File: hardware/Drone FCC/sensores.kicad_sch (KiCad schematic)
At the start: 12 parts, among them J1 Mag Dupont, J19 GPS M8N - DF13, J2 GPS Dupont, J20 Mag DF13, U1 ICM-42688-V, U2 ILPS22QSTR

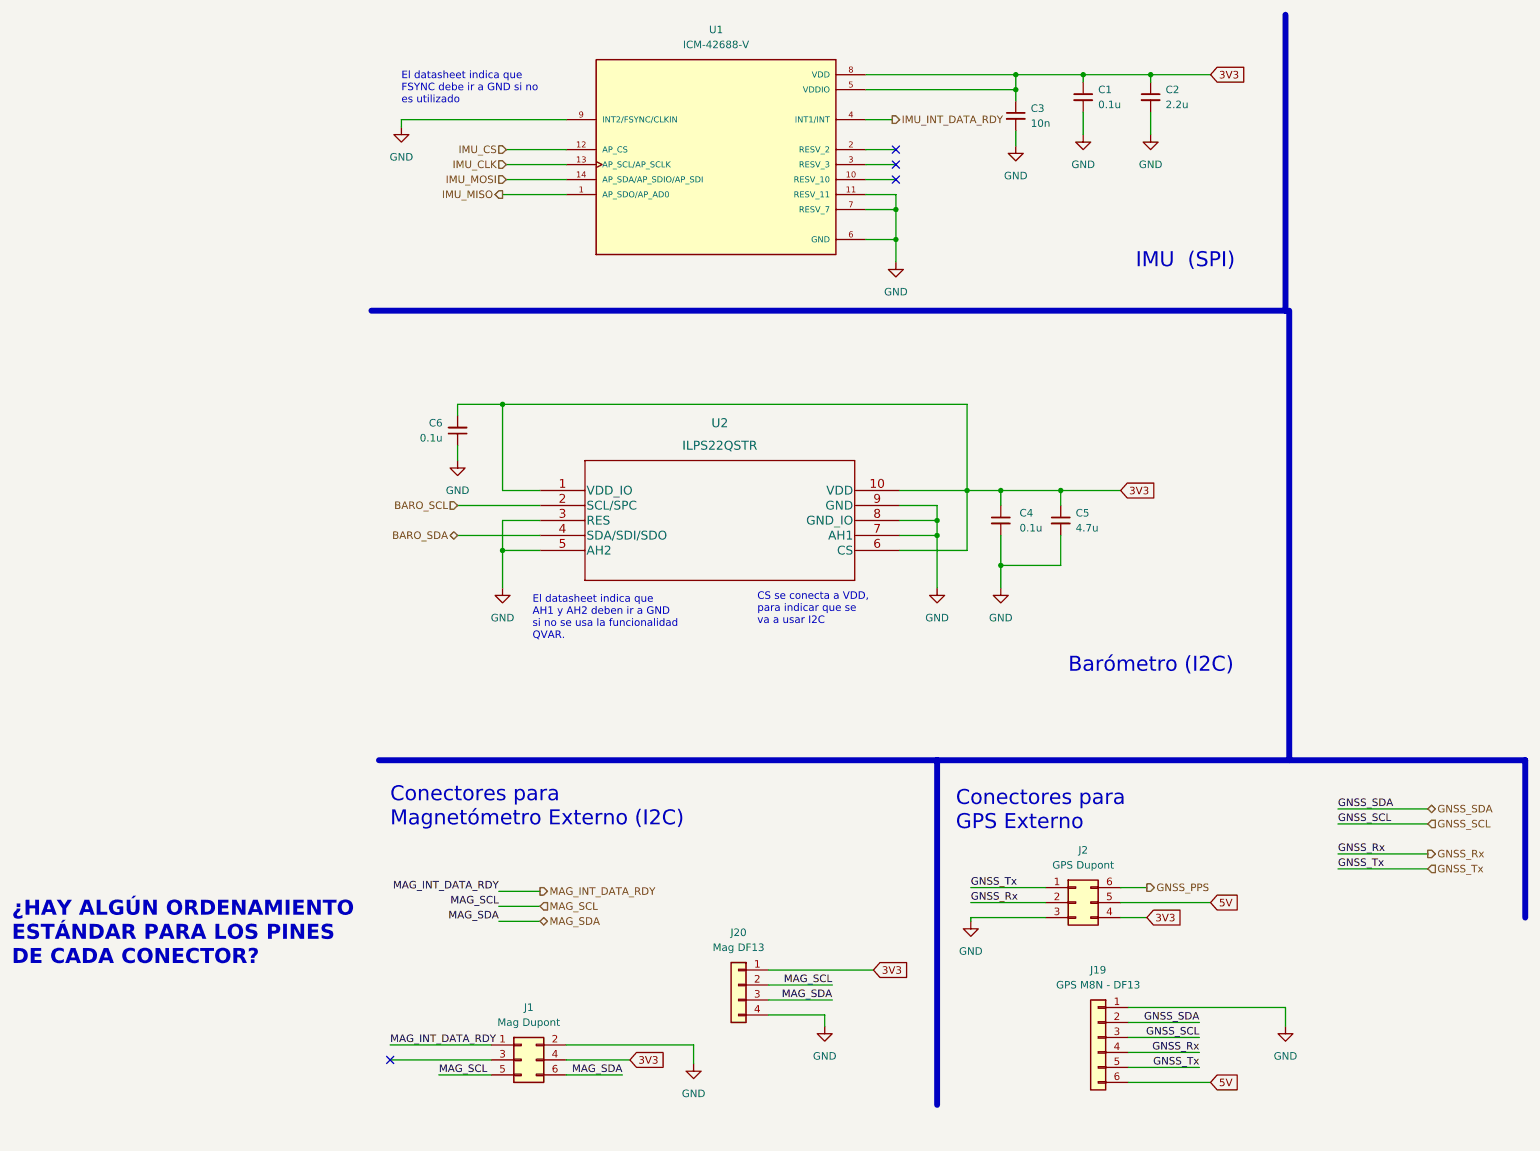
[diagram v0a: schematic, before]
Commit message: re enumeration of components
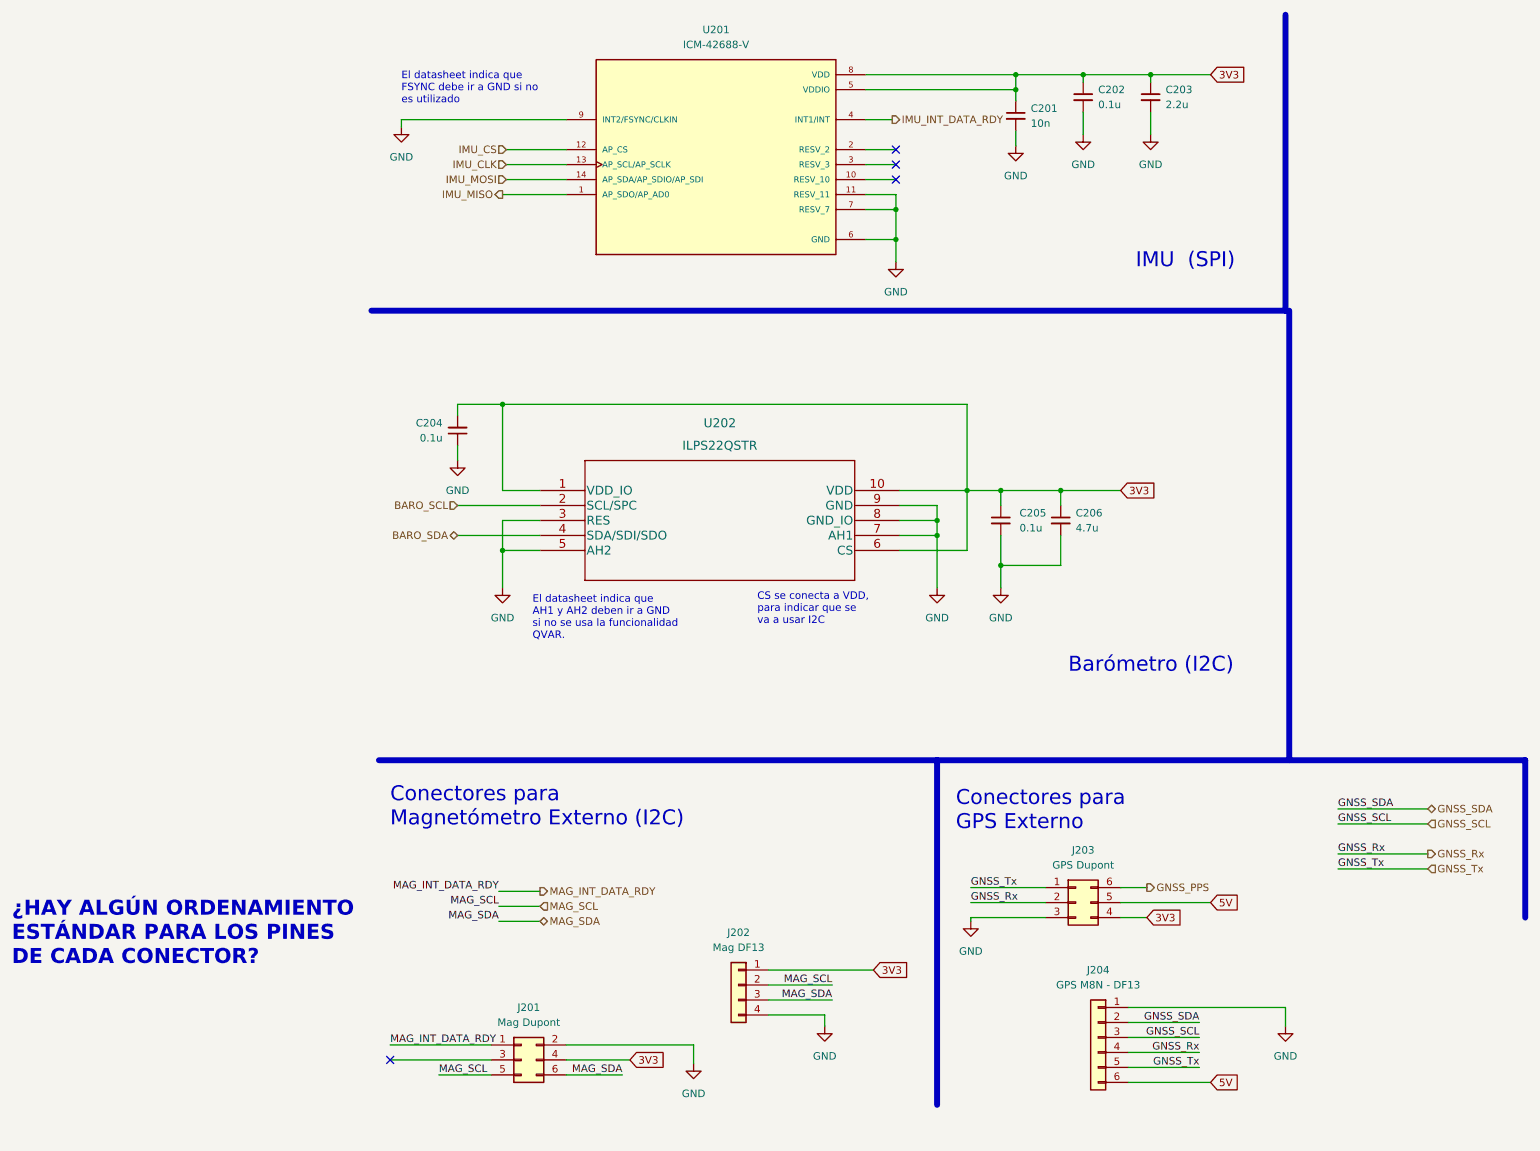
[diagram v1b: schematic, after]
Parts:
- C201: renamed from C3; footprint (none) -> Capacitor_SMD:C_0603_1608Metric_Pad1.08x0.95mm_HandSolder
- C202: renamed from C1; footprint (none) -> Capacitor_SMD:C_0603_1608Metric_Pad1.08x0.95mm_HandSolder
- C203: renamed from C2; footprint (none) -> Capacitor_SMD:C_0603_1608Metric_Pad1.08x0.95mm_HandSolder
- C204: renamed from C6; footprint (none) -> Capacitor_SMD:C_0603_1608Metric_Pad1.08x0.95mm_HandSolder
- C205: renamed from C4; footprint (none) -> Capacitor_SMD:C_0603_1608Metric_Pad1.08x0.95mm_HandSolder
- C206: renamed from C5; footprint (none) -> Capacitor_SMD:C_0805_2012Metric_Pad1.18x1.45mm_HandSolder
- renumbered J1 to J201, J20 to J202, J2 to J203, J19 to J204, U1 to U201, U2 to U202
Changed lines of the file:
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@@
   (symbol (lib_id "Connector_Generic:Conn_02x03_Odd_Even") (at 37.465 189.23 0) (unit 1)
     (in_bom yes) (on_board yes) (fields_autoplaced)
-    (property "Reference" "J1" (id 0) (at 38.735 180.34 0))
+    (property "Reference" "J201" (id 0) (at 38.735 180.34 0))
     (property "Value" "Mag Dupont" (id 1) (at 38.735 182.88 0))
     (property "Footprint" "Connector_PinHeader_2.54mm:PinHeader_2x03_P2.54mm_Horizontal" (id 2) (at 37.465 189.23 0)
@@
   (symbol (lib_id "Device:C_Small") (at 128.905 97.79 0) (unit 1)
     (in_bom yes) (on_board yes) (fields_autoplaced)
-    (property "Reference" "C5" (id 0) (at 131.445 96.5262 0)
+    (property "Reference" "C206" (id 0) (at 131.445 96.5262 0)
       (effects (font (size 1.27 1.27)) (justify left))
     )
@@
       (effects (font (size 1.27 1.27)) (justify left))
     )
-    (property "Footprint" "" (id 2) (at 128.905 97.79 0)
+    (property "Footprint" "Capacitor_SMD:C_0805_2012Metric_Pad1.18x1.45mm_HandSolder" (id 2) (at 128.905 97.79 0)
       (effects (font (size 1.27 1.27)) hide)
     )
@@
   (symbol (lib_id "Connector_Generic:Conn_01x04") (at 74.295 176.53 0) (mirror y) (unit 1)
     (in_bom yes) (on_board yes) (fields_autoplaced)
-    (property "Reference" "J20" (id 0) (at 74.295 167.64 0))
+    (property "Reference" "J202" (id 0) (at 74.295 167.64 0))
     (property "Value" "Mag DF13" (id 1) (at 74.295 170.18 0))
     (property "Footprint" "Connector_Hirose:Hirose_DF13C_CL535-0404-8-51_1x04-1MP_P1.25mm_Vertical" (id 2) (at 74.295 176.53 0)
@@
   (symbol (lib_id "ICM-42688-V:ICM-42688-V") (at 70.485 34.925 0) (unit 1)
     (in_bom yes) (on_board yes) (fields_autoplaced)
-    (property "Reference" "U1" (id 0) (at 70.485 14.605 0))
+    (property "Reference" "U201" (id 0) (at 70.485 14.605 0))
     (property "Value" "ICM-42688-V" (id 1) (at 70.485 17.145 0))
     (property "Footprint" "ICM-42688-V:PQFN50P300X250X97-14N" (id 2) (at 70.485 34.925 0)
@@
   (symbol (lib_id "ILPS22QSTR:ILPS22QSTR") (at 40.64 92.71 0) (unit 1)
     (in_bom yes) (on_board yes) (fields_autoplaced)
-    (property "Reference" "U2" (id 0) (at 71.12 81.28 0)
+    (property "Reference" "U202" (id 0) (at 71.12 81.28 0)
       (effects (font (size 1.524 1.524)))
     )
@@
   (symbol (lib_id "Device:C_Small") (at 144.145 26.035 0) (unit 1)
     (in_bom yes) (on_board yes) (fields_autoplaced)
-    (property "Reference" "C2" (id 0) (at 146.685 24.7712 0)
+    (property "Reference" "C203" (id 0) (at 146.685 24.7712 0)
       (effects (font (size 1.27 1.27)) (justify left))
     )
@@
       (effects (font (size 1.27 1.27)) (justify left))
     )
-    (property "Footprint" "" (id 2) (at 144.145 26.035 0)
+    (property "Footprint" "Capacitor_SMD:C_0603_1608Metric_Pad1.08x0.95mm_HandSolder" (id 2) (at 144.145 26.035 0)
       (effects (font (size 1.27 1.27)) hide)
     )
@@
   (symbol (lib_id "Device:C_Small") (at 132.715 26.035 0) (unit 1)
     (in_bom yes) (on_board yes) (fields_autoplaced)
-    (property "Reference" "C1" (id 0) (at 135.255 24.7712 0)
+    (property "Reference" "C202" (id 0) (at 135.255 24.7712 0)
       (effects (font (size 1.27 1.27)) (justify left))
     )
@@
       (effects (font (size 1.27 1.27)) (justify left))
     )
-    (property "Footprint" "" (id 2) (at 132.715 26.035 0)
+    (property "Footprint" "Capacitor_SMD:C_0603_1608Metric_Pad1.08x0.95mm_HandSolder" (id 2) (at 132.715 26.035 0)
       (effects (font (size 1.27 1.27)) hide)
     )
@@
   (symbol (lib_id "Device:C_Small") (at 26.67 82.55 0) (mirror x) (unit 1)
     (in_bom yes) (on_board yes) (fields_autoplaced)
-    (property "Reference" "C6" (id 0) (at 24.13 81.2735 0)
+    (property "Reference" "C204" (id 0) (at 24.13 81.2735 0)
       (effects (font (size 1.27 1.27)) (justify right))
     )
@@
       (effects (font (size 1.27 1.27)) (justify right))
     )
-    (property "Footprint" "" (id 2) (at 26.67 82.55 0)
+    (property "Footprint" "Capacitor_SMD:C_0603_1608Metric_Pad1.08x0.95mm_HandSolder" (id 2) (at 26.67 82.55 0)
       (effects (font (size 1.27 1.27)) hide)
     )
@@
   (symbol (lib_id "Device:C_Small") (at 121.285 29.21 0) (unit 1)
     (in_bom yes) (on_board yes) (fields_autoplaced)
-    (property "Reference" "C3" (id 0) (at 123.825 27.9462 0)
+    (property "Reference" "C201" (id 0) (at 123.825 27.9462 0)
       (effects (font (size 1.27 1.27)) (justify left))
     )
@@
       (effects (font (size 1.27 1.27)) (justify left))
     )
-    (property "Footprint" "" (id 2) (at 121.285 29.21 0)
+    (property "Footprint" "Capacitor_SMD:C_0603_1608Metric_Pad1.08x0.95mm_HandSolder" (id 2) (at 121.285 29.21 0)
       (effects (font (size 1.27 1.27)) hide)
     )
@@
   (symbol (lib_id "Connector_Generic:Conn_02x03_Counter_Clockwise") (at 131.445 162.56 0) (unit 1)
     (in_bom yes) (on_board yes) (fields_autoplaced)
-    (property "Reference" "J2" (id 0) (at 132.715 153.67 0))
+    (property "Reference" "J203" (id 0) (at 132.715 153.67 0))
     (property "Value" "GPS Dupont" (id 1) (at 132.715 156.21 0))
     (property "Footprint" "Connector_PinHeader_2.54mm:PinHeader_2x03_P2.54mm_Horizontal" (id 2) (at 131.445 162.56 0)
@@
   (symbol (lib_id "Connector_Generic:Conn_01x06") (at 135.255 185.42 0) (mirror y) (unit 1)
     (in_bom yes) (on_board yes) (fields_autoplaced)
-    (property "Reference" "J19" (id 0) (at 135.255 173.99 0))
+    (property "Reference" "J204" (id 0) (at 135.255 173.99 0))
     (property "Value" "GPS M8N - DF13" (id 1) (at 135.255 176.53 0))
     (property "Footprint" "Connector_Hirose:Hirose_DF13C_CL535-0406-3-51_1x06-1MP_P1.25mm_Vertical" (id 2) (at 135.255 185.42 0)
@@
   (symbol (lib_id "Device:C_Small") (at 118.745 97.79 0) (unit 1)
     (in_bom yes) (on_board yes) (fields_autoplaced)
-    (property "Reference" "C4" (id 0) (at 121.92 96.5262 0)
+    (property "Reference" "C205" (id 0) (at 121.92 96.5262 0)
       (effects (font (size 1.27 1.27)) (justify left))
     )
@@
       (effects (font (size 1.27 1.27)) (justify left))
     )
-    (property "Footprint" "" (id 2) (at 118.745 97.79 0)
-      (effects (font (size 1.27 1.27)) hide)
-    )
+    (property "Footprint" "Capacitor_SMD:C_0603_1608Metric_Pad1.08x0.95mm_HandSolder" (id 2) (at 118.745 97.79 0)
+      (effects (font (size 1.27 1.27)) hide)
+    )

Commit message: start routing
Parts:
- removed J202: Mag DF13, Connector_Hirose:Hirose_DF13C_CL535-0404-8-51_1x04-1MP_P1.25mm_Vertical, symbol Connector_Generic:Conn_01x04
- removed J204: GPS M8N - DF13, Connector_Hirose:Hirose_DF13C_CL535-0406-3-51_1x06-1MP_P1.25mm_Vertical, symbol Connector_Generic:Conn_01x06
- added J202: Mag DF13, Connector_Hirose:Hirose_DF13C_CL535-0404-8-51_1x04-1MP_P1.25mm_Vertical, symbol DF13C-4P-1.25V(51):DF13C-4P-1.25V(51)
- added J204: GPS M8N - DF13, DF13C-6P-1.25V(51):HIROSE_DF13C-6P-1.25V(51), symbol DF13C-69-1.25v(51):DF13C-6P-1.25V(51)
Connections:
- net 3V3: now also J202.1
- net 5V: now also J204.6
- net GND: now also J202.4, J202.MP, J204.1, J204.S1 (SHIELD), J204.S2 (SHIELD)
- net GNSS_Rx: now also J204.4
- net GNSS_SCL: now also J204.3
- net GNSS_SDA: now also J204.2
- net GNSS_Tx: now also J204.5
- net MAG_SCL: now also J202.2
- net MAG_SDA: now also J202.3
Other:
- moved on the sheet: J203
